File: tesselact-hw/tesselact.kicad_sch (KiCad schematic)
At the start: 40 parts, among them J1 Screw_Terminal_01x02, J2 USB_B_Micro, J3 Conn_ARM_JTAG_SWD_10, J4 Conn_01x08_Female, J5 Conn_01x08_Female, U1 BQ24072RGT, U2 TPS73633DBV, U3 USBLC6-2SC6, U4 STM32L052R8Tx, U5 LIS3DH

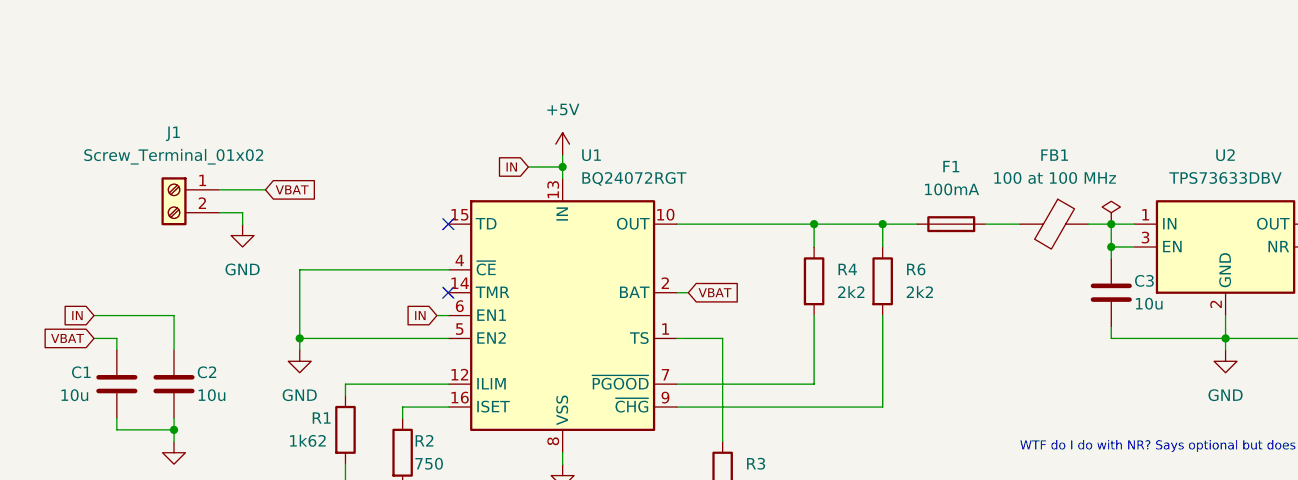
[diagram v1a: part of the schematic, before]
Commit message: Assigned footprints and removed fuse
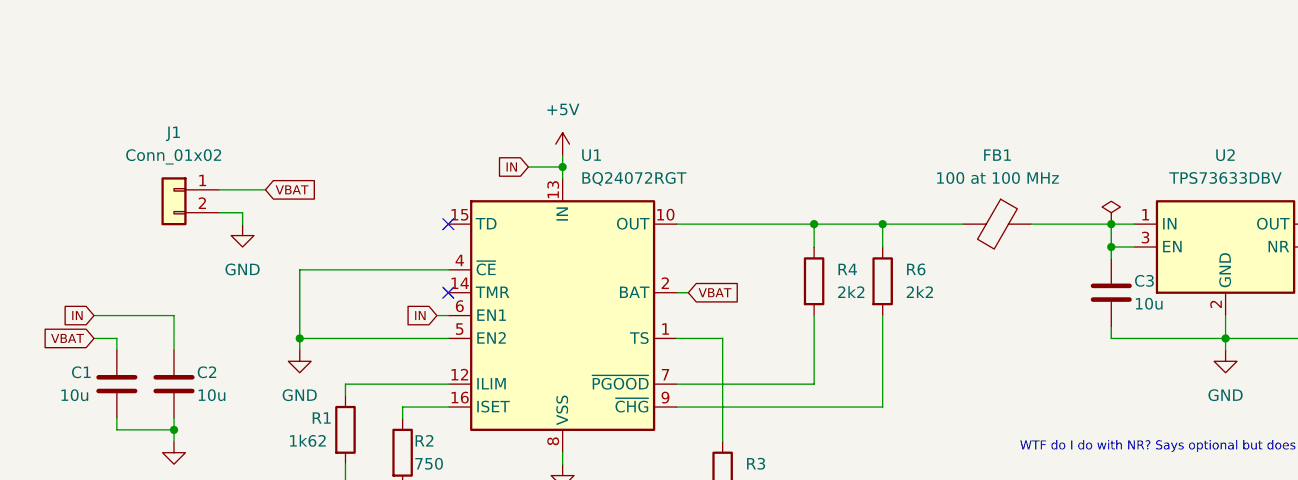
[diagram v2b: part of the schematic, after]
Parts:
- removed F1: 100mA, symbol Device:Fuse
- removed J1: Screw_Terminal_01x02, symbol Connector:Screw_Terminal_01x02
- added J1: Conn_01x02, Connector_JST:JST_XH_B2B-XH-A_1x02_P2.50mm_Vertical, symbol Connector_Generic:Conn_01x02
- C1, C2, C3, C4: footprint (none) -> Capacitor_SMD:C_0603_1608Metric
- C10, C11, C12, C5, C6, C7, C8, C9: footprint (none) -> Capacitor_SMD:C_0402_1005Metric
- FB1: footprint (none) -> Inductor_SMD:L_0603_1608Metric
- J2: footprint (none) -> Connector_USB:USB_Micro-B_Wuerth_629105150521
- J3: footprint (none) -> Connector_PinHeader_1.27mm:PinHeader_2x05_P1.27mm_Vertical_SMD
- J4, J5: footprint (none) -> Connector_PinSocket_2.54mm:PinSocket_1x08_P2.54mm_Vertical
- R1, R10, R11, R12, R13, R14, R15, R16, R17, R18, R2, R3, R4, R5, R6, R7: footprint (none) -> Resistor_SMD:R_0402_1005Metric
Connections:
- net GND: now also J1.2 (Pin_2)
- net VBAT: now also J1.1 (Pin_1)
- net at R4.1, R6.1, U1.10 (OUT)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: now also FB1.2
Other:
- moved on the sheet: FB1

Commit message: Update title block data
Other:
- title: (none) -> tesselact
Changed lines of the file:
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@@
 (kicad_sch (version 20211123) (generator eeschema)
   (paper "A4")
+  (title_block
+    (title "tesselact")
+    (date "2022-10-13")
+    (rev "0.1.0")
+  )
   (junction (at 238.76 50.8) (diameter 0) (color 0 0 0 0)
   )
